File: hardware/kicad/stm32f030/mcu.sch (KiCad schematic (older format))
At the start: 14 parts, among them P10 SWD, P8 UART, P9 I2C, SW3 SW_Push, U2 STM32F030F4Px, Y1 8MHz

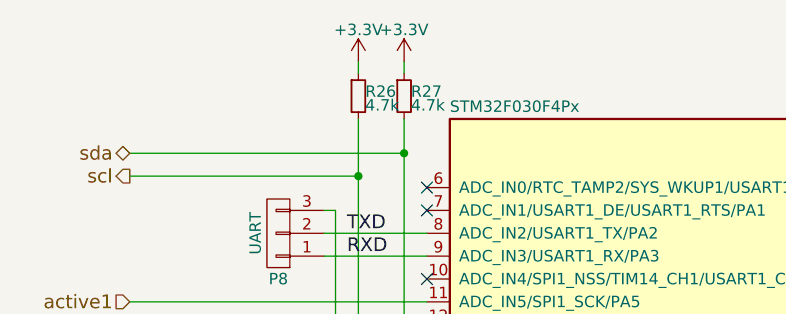
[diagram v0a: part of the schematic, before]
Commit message: hardware/kicad/stm32f030: changed i2c bus and eeprom voltage to 5V
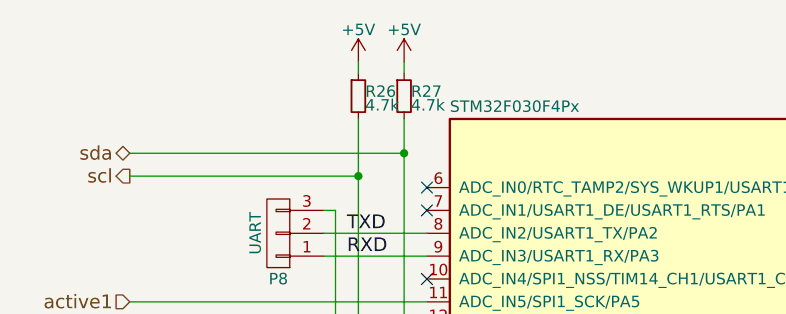
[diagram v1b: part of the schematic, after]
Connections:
- net +3V3: no longer R26.1, R27.1
- new net +5V: R26.1, R27.1
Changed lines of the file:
@@
 $Comp
 L +3.3V #PWR042
-U 1 1 58855640
-P 4050 2600
-F 0 "#PWR042" H 4050 2450 50  0001 C CNN
-F 1 "+3.3V" H 4050 2740 50  0000 C CNN
-F 2 "" H 4050 2600 50  0000 C CNN
-F 3 "" H 4050 2600 50  0000 C CNN
-	1    4050 2600
-	1    0    0    -1
-$EndComp
-$Comp
-L +3.3V #PWR043
-U 1 1 5885566F
-P 4250 2600
-F 0 "#PWR043" H 4250 2450 50  0001 C CNN
-F 1 "+3.3V" H 4250 2740 50  0000 C CNN
-F 2 "" H 4250 2600 50  0000 C CNN
-F 3 "" H 4250 2600 50  0000 C CNN
-	1    4250 2600
-	1    0    0    -1
-$EndComp
-$Comp
-L +3.3V #PWR044
 U 1 1 5885595B
 P 8550 3750
-F 0 "#PWR044" H 8550 3600 50  0001 C CNN
+F 0 "#PWR042" H 8550 3600 50  0001 C CNN
 F 1 "+3.3V" H 8550 3890 50  0000 C CNN
 F 2 "" H 8550 3750 50  0000 C CNN
@@
 	1    0    0    -1
 $EndComp
+$Comp
+L +5V #PWR043
+U 1 1 58BC205D
+P 4050 2600
+F 0 "#PWR043" H 4050 2450 50  0001 C CNN
+F 1 "+5V" H 4050 2740 50  0000 C CNN
+F 2 "" H 4050 2600 50  0001 C CNN
+F 3 "" H 4050 2600 50  0001 C CNN
+	1    4050 2600
+	1    0    0    -1
+$EndComp
+$Comp
+L +5V #PWR044
+U 1 1 58BC208D
+P 4250 2600
+F 0 "#PWR044" H 4250 2450 50  0001 C CNN
+F 1 "+5V" H 4250 2740 50  0000 C CNN
+F 2 "" H 4250 2600 50  0001 C CNN
+F 3 "" H 4250 2600 50  0001 C CNN
+	1    4250 2600
+	1    0    0    -1
+$EndComp
